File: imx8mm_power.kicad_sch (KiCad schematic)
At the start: 38 parts, among them U1 MIMX8MM6DVTLZAA

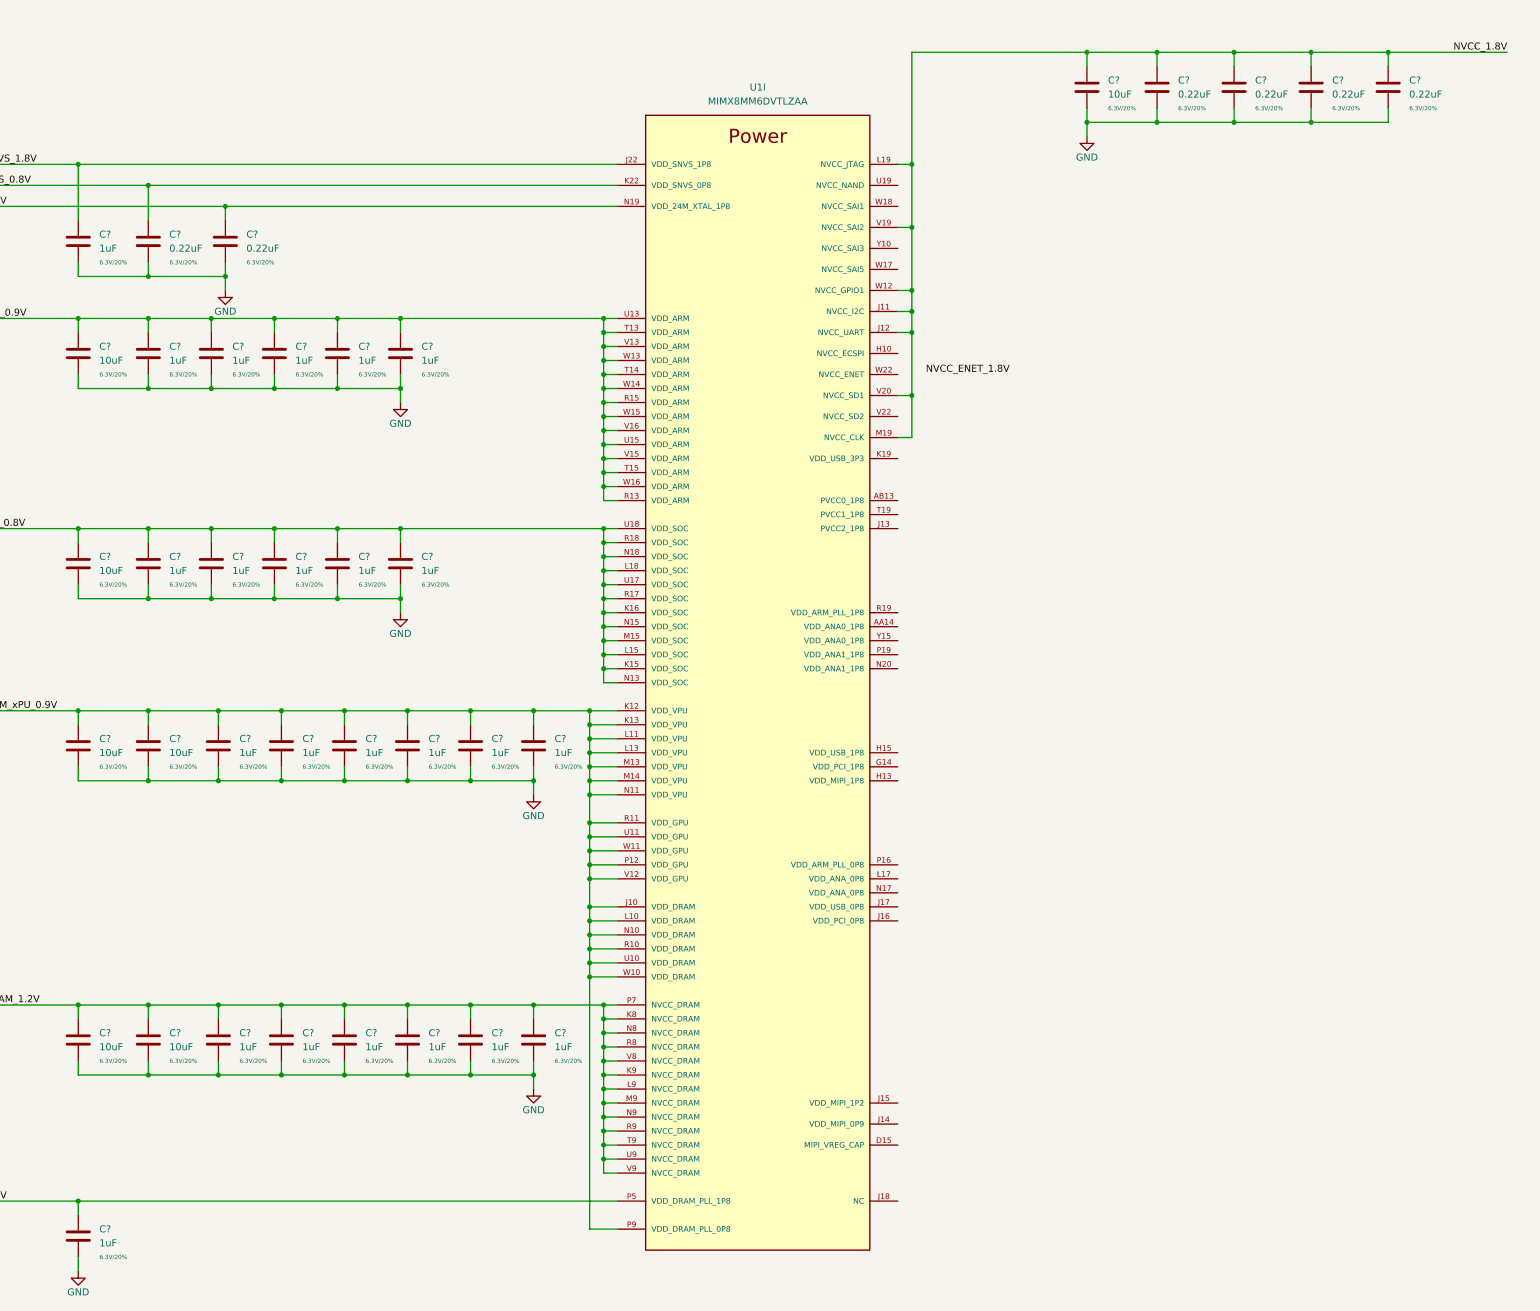
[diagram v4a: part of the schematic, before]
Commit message: pcie done, misc fixes for usb, enet
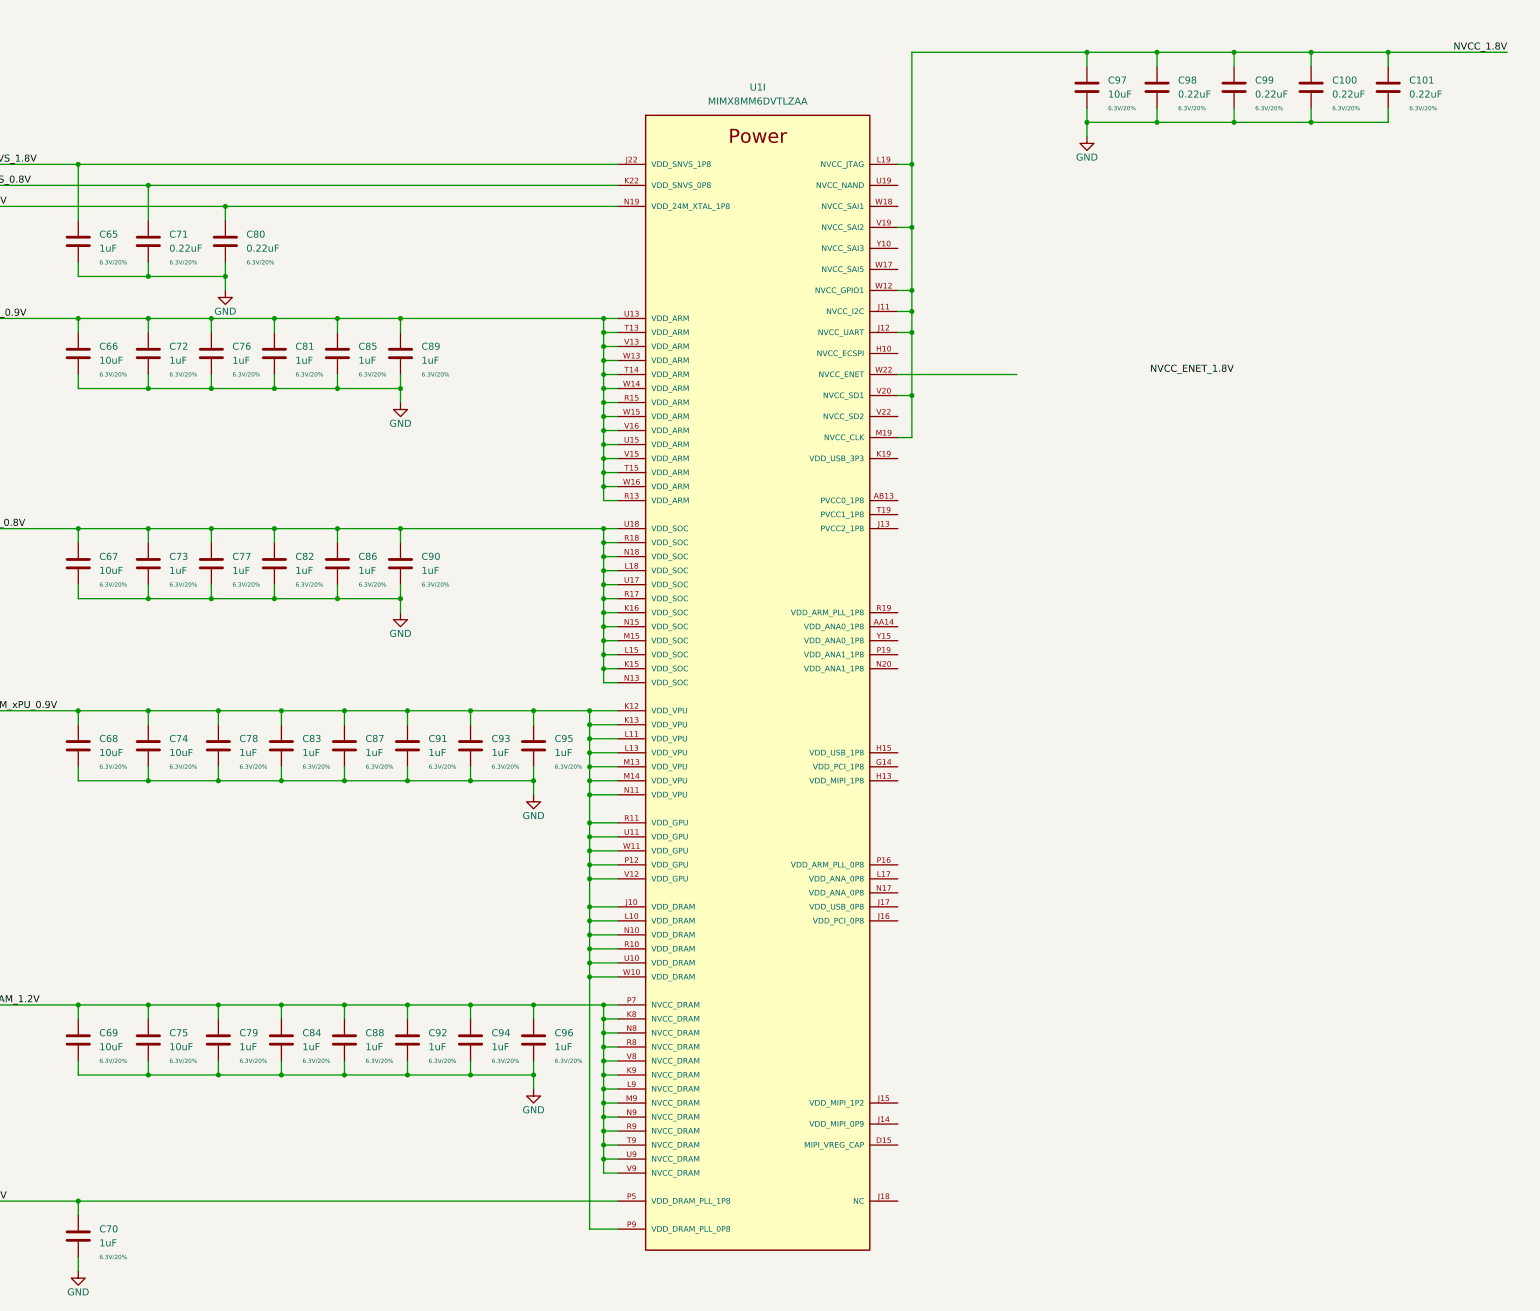
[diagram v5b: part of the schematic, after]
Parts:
- gave numbers to parts that had none: 37

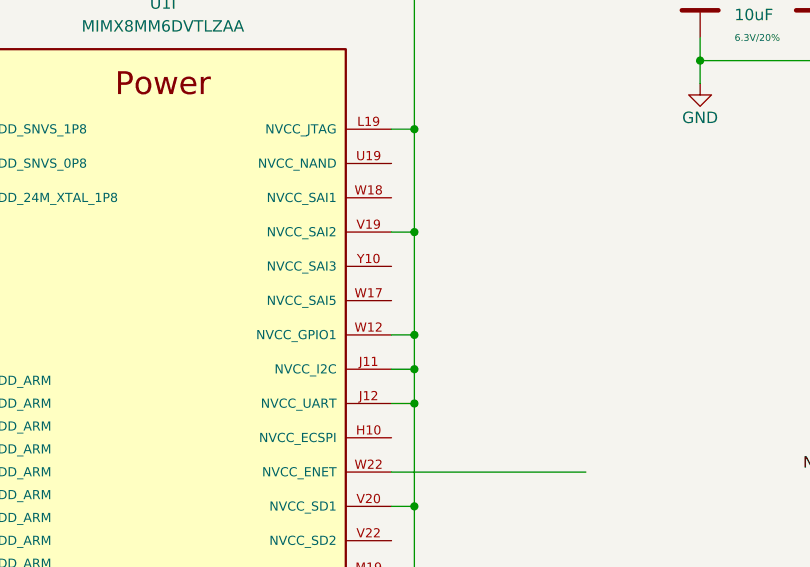
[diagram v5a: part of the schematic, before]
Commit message: storage done, peri work, misc fixes
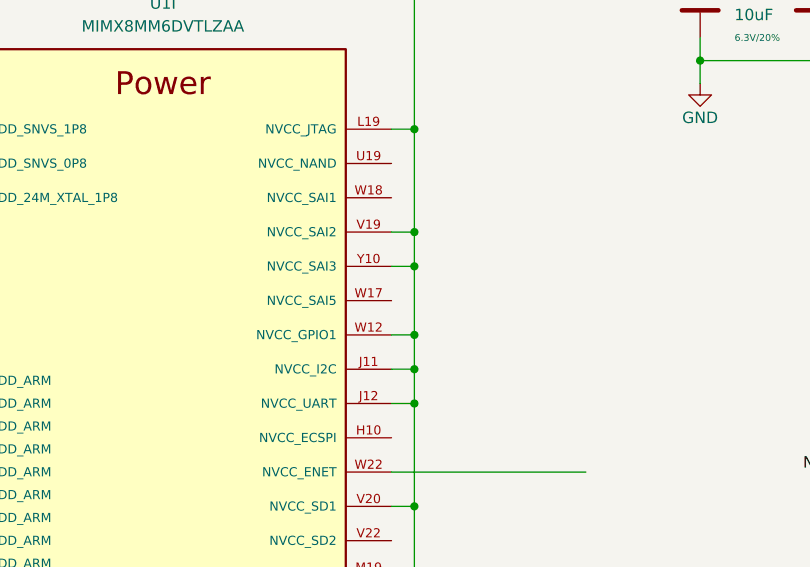
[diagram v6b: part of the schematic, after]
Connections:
- net NVCC_1.8V: now also U1.Y10 (NVCC_SAI3)
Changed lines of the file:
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@@
   (junction (at 158.75 74.93) (diameter 0) (color 0 0 0 0)
   )
+  (junction (at 214.63 62.23) (diameter 0) (color 0 0 0 0)
+  )
   (junction (at 63.5 146.05) (diameter 0) (color 0 0 0 0)
   )
@@
     (stroke (width 0) (type default) (color 0 0 0 0))
   )
-  (wire (pts (xy 214.63 58.42) (xy 214.63 69.85))
+  (wire (pts (xy 214.63 58.42) (xy 214.63 62.23))
     (stroke (width 0) (type default) (color 0 0 0 0))
   )
@@
     (stroke (width 0) (type default) (color 0 0 0 0))
   )
+  (wire (pts (xy 212.09 62.23) (xy 214.63 62.23))
+    (stroke (width 0) (type default) (color 0 0 0 0))
+  )
   (wire (pts (xy 337.82 229.87) (xy 340.36 229.87))
     (stroke (width 0) (type default) (color 0 0 0 0))
@@
     (stroke (width 0) (type default) (color 0 0 0 0))
   )
+  (wire (pts (xy 214.63 62.23) (xy 214.63 69.85))
+    (stroke (width 0) (type default) (color 0 0 0 0))
+  )

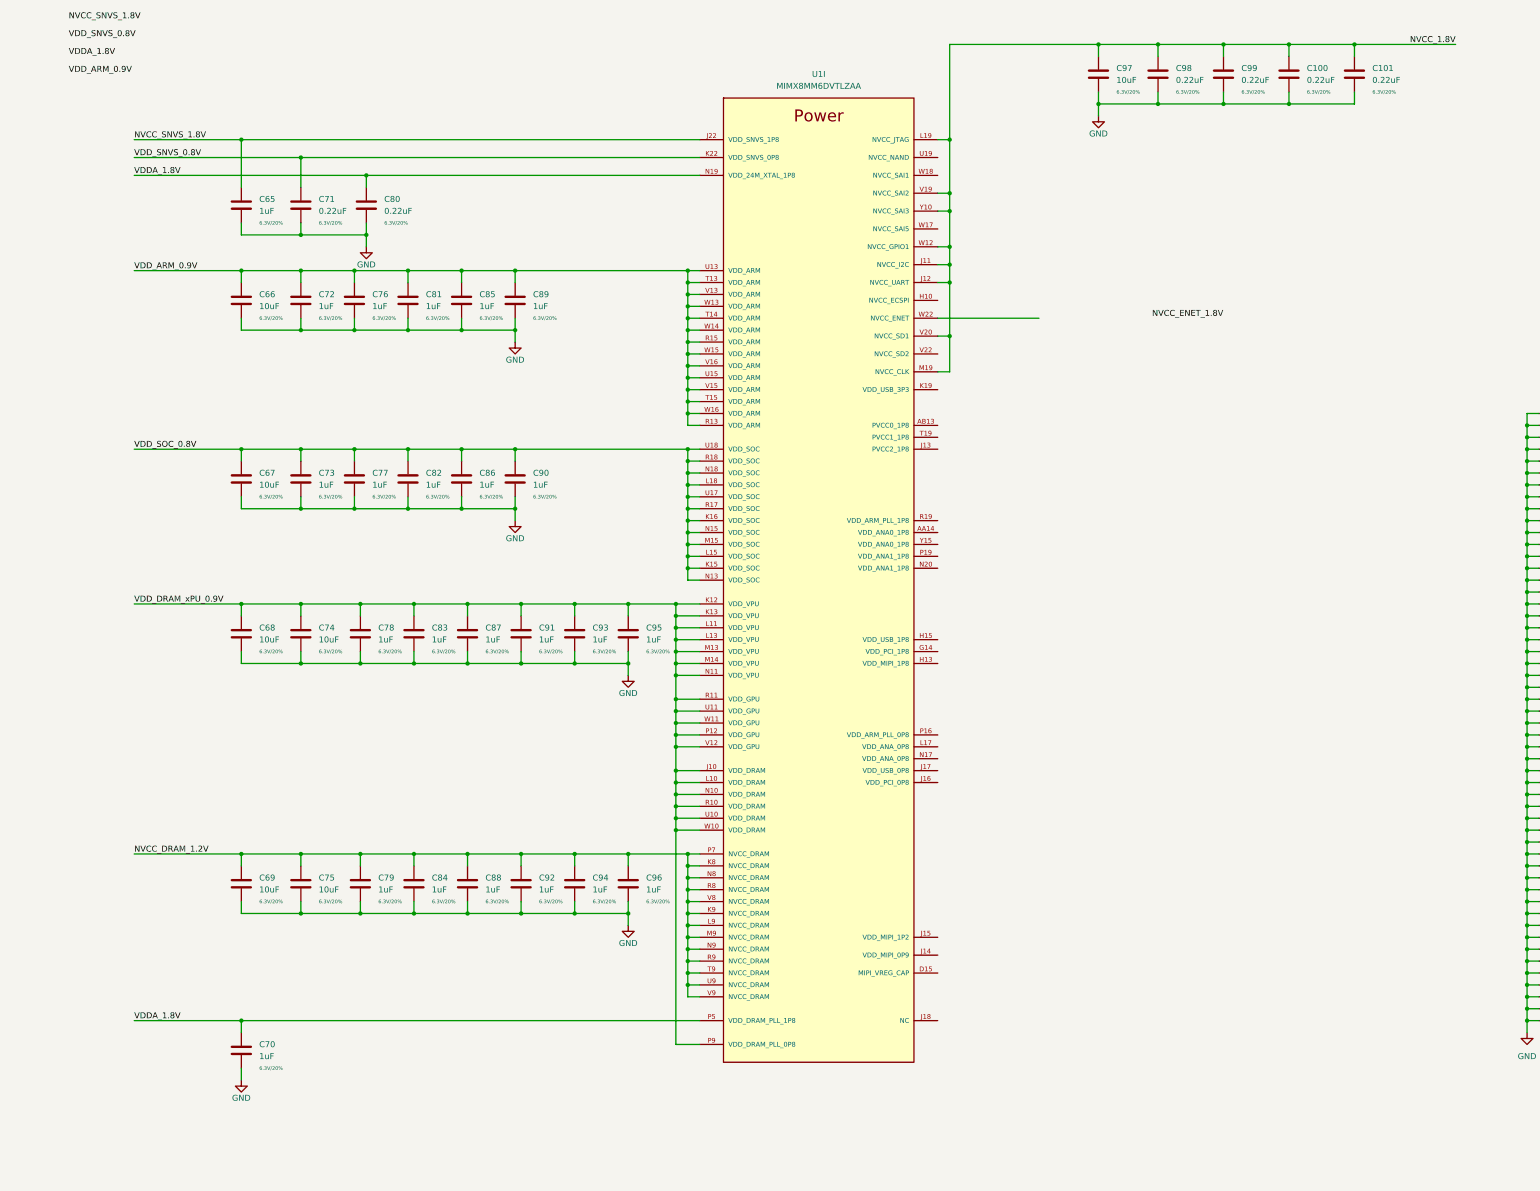
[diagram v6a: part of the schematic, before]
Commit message: ddr: add dual die support, misc work
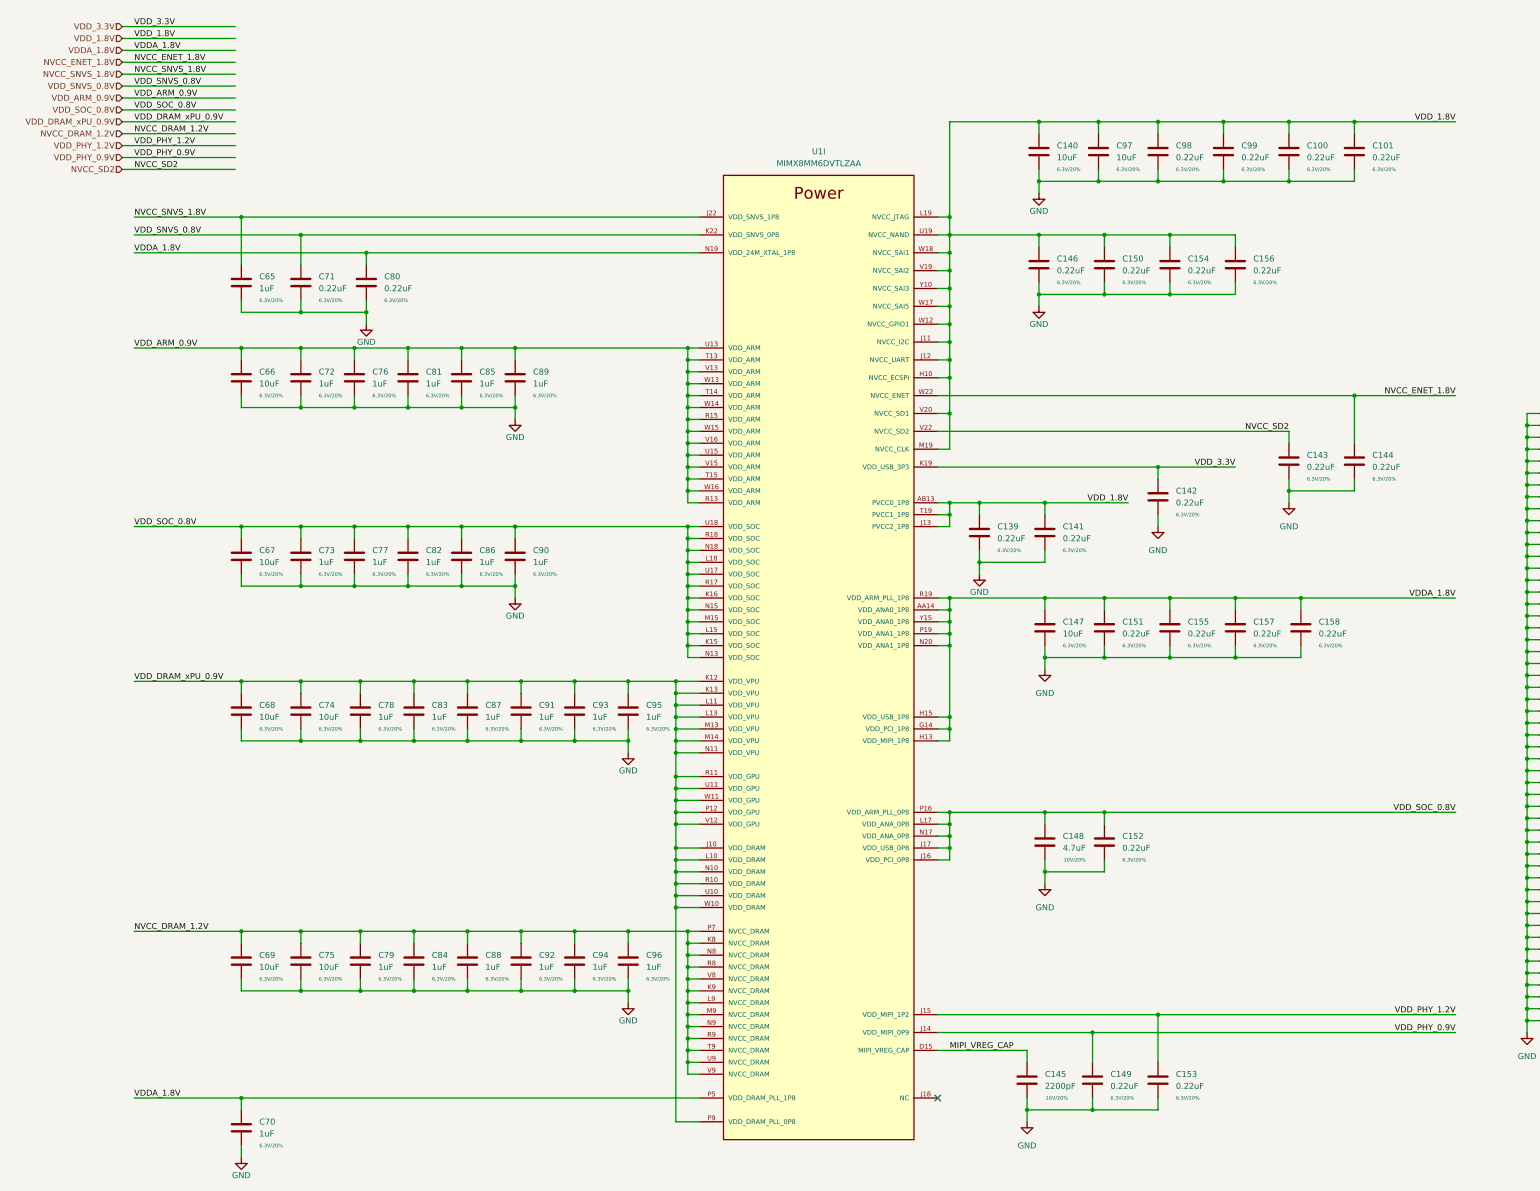
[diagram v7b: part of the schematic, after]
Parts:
- added C139, C141, C142, C143, C144, C146, C149, C150, C151, C152, C153, C154, C155, C156, C157, C158: 0.22uF, Capacitor_SMD:C_0201_0603Metric, symbol Device:C
- added C140, C147: 10uF, Capacitor_SMD:C_0402_1005Metric, symbol Device:C
- added C145: 2200pF, Capacitor_SMD:C_0402_1005Metric, symbol Device:C
- added C148: 4.7uF, Capacitor_SMD:C_0402_1005Metric, symbol Device:C
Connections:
- net NVCC_1.8V is gone; now on net VDD_1.8V: C100.1, C101.1, C97.1, C98.1, C99.1, U1.J11 (NVCC_I2C), U1.J12 (NVCC_UART), U1.L19 (NVCC_JTAG), U1.M19 (NVCC_CLK), U1.V19 (NVCC_SAI2), U1.V20 (NVCC_SD1), U1.W12 (NVCC_GPIO1), U1.Y10 (NVCC_SAI3)
- net GND: now also C139.2, C140.2, C141.2, C142.2, C143.2, C144.2, C145.2, C146.2, C147.2, C148.2, C149.2, C150.2, C151.2, C152.2, C153.2, C154.2, C155.2, C156.2, C157.2, C158.2
- net NVCC_ENET_1.8V: now also U1.W22 (NVCC_ENET), C144.1
- net VDDA_1.8V: now also U1.AA14 (VDD_ANA0_1P8), U1.G14 (VDD_PCI_1P8), U1.H13 (VDD_MIPI_1P8), U1.H15 (VDD_USB_1P8), U1.N20 (VDD_ANA1_1P8), U1.P19 (VDD_ANA1_1P8), U1.R19 (VDD_ARM_PLL_1P8), U1.Y15 (VDD_ANA0_1P8), C147.1, C151.1, C155.1, C157.1, C158.1
- net VDD_SOC_0.8V: now also U1.J16 (VDD_PCI_0P8), U1.J17 (VDD_USB_0P8), U1.L17 (VDD_ANA_0P8), U1.N17 (VDD_ANA_0P8), U1.P16 (VDD_ARM_PLL_0P8), C148.1, C152.1
- net VDD_1.8V: now reaches U1.AB13 (PVCC0_1P8)
- net VDD_1.8V: now also U1.H10 (NVCC_ECSPI), U1.J13 (PVCC2_1P8), U1.T19 (PVCC1_1P8), U1.U19 (NVCC_NAND), U1.W17 (NVCC_SAI5), U1.W18 (NVCC_SAI1), C139.1, C140.1, C141.1, C146.1, C150.1, C154.1, C156.1
- net MIPI_VREG_CAP: now reaches U1.D15 (MIPI_VREG_CAP)
- net MIPI_VREG_CAP: now also C145.1
- net VDD_PHY_0.9V: now reaches U1.J14 (VDD_MIPI_0P9)
- net VDD_PHY_0.9V: now also C149.1
- net VDD_PHY_1.2V: now reaches U1.J15 (VDD_MIPI_1P2)
- net VDD_PHY_1.2V: now also C153.1
- net VDD_3.3V: now reaches U1.K19 (VDD_USB_3P3)
- net VDD_3.3V: now also C142.1
- net NVCC_SD2: now reaches U1.V22 (NVCC_SD2)
- net NVCC_SD2: now also C143.1
- no-connect marks 0 -> 1
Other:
- company: (none) -> Q-LAB
- title: (none) -> QSBC
- moved on the sheet: C100, C101, C65, C66, C67, C68, C69, C70, C71, C72, C73, C74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
